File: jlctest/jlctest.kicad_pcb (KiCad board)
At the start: 2 copper layers, 121 x 75.5 mm, 44 parts, among them Q1 MMBT5551_C2145, Q2 S8550_C105432, Q3 SI2301CDS-T1-GE3, Q4 AO3401A, Q5 D882_C9634, SW1 TS-1187A-B-A-B, U1 OP07CDR, U10 L78M05ABDT-TR, U2 TPS5430DDAR, U3 SP485EEN-L/TR, U4 W25Q128JVSIQTR, U5 LM324DT, U6 74HC595D,118, U7 SP3232EEY-L/TR, U8 AMS1117-3.3, U9 AMS1117-5.0, X1 X322516MLB4SI, X2 Q13FC1350000400, X3 X322512MSB4SI, X4 X49SM8MSD2SC, X5 X50328MSB2GI

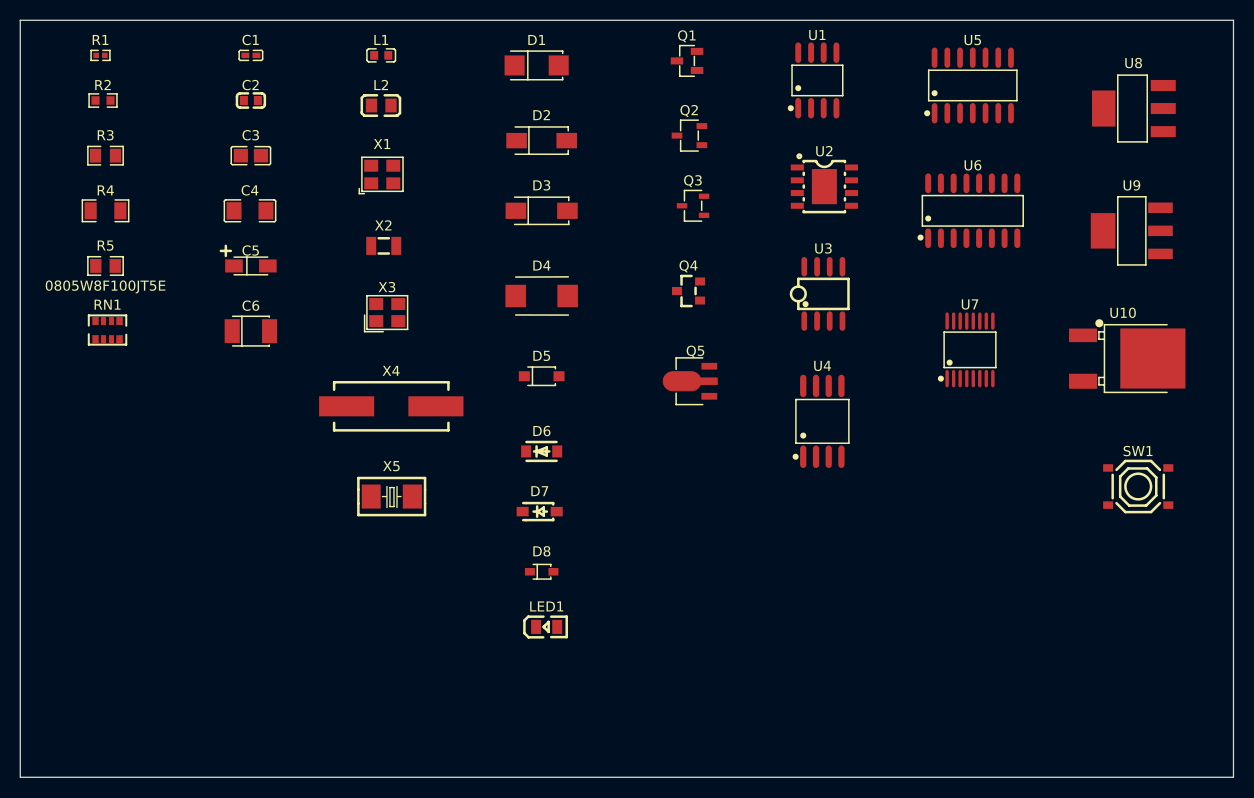
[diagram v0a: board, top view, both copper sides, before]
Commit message: Used (extends) on all symbols having an identical set of child symbols
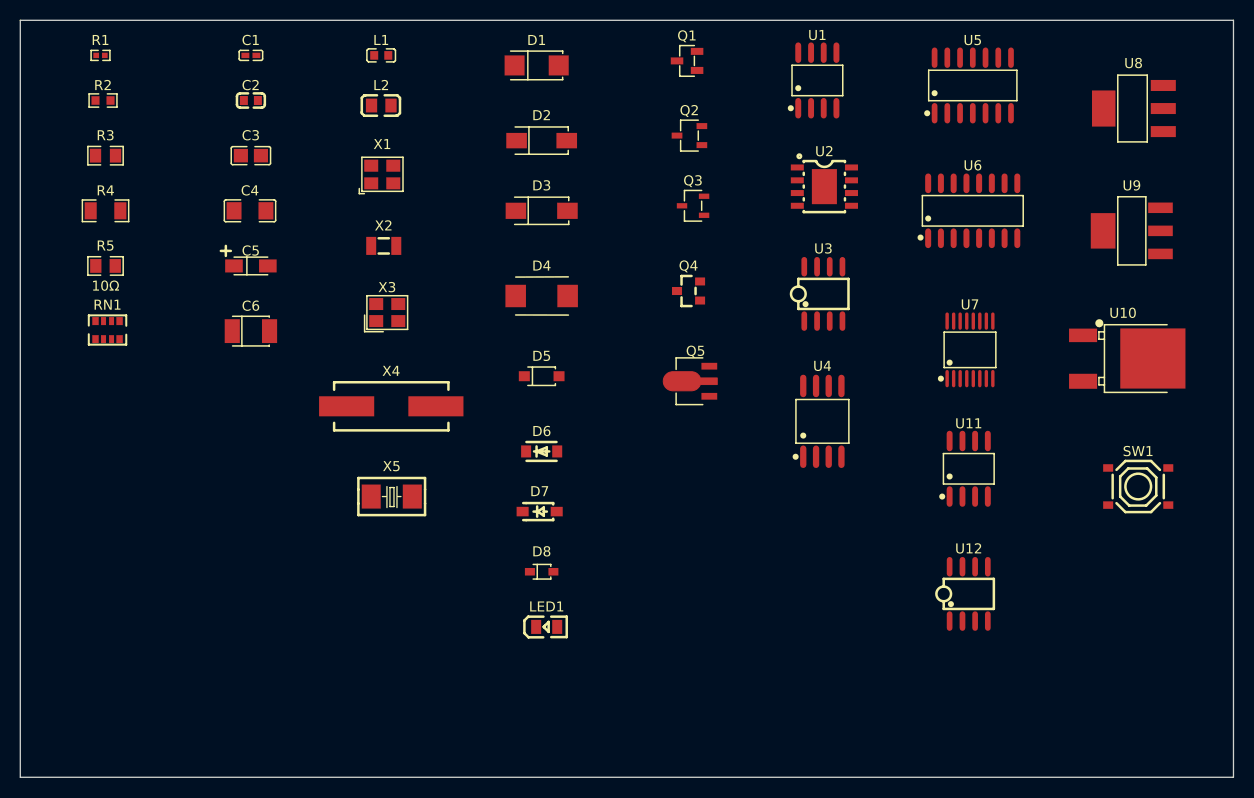
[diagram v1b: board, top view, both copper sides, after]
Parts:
- added U11: NE5532DR, jlcbasic:SOIC-8_L4.9-W3.9-P1.27-LS6.0-BL, F.Cu at (200.6, 112.7)
- added U12: TL072CDT, jlcbasic:SOIC-8_L5.0-W4.0-P1.27-LS6.0-BL, F.Cu at (200.6, 125.2)
- C1: value 0402B102K500NT -> 1nF
- C2: value 0603B103K500NT -> 10nF
- C3: value 0805B333K500NT -> 33nF
- C4: value 1206B102K202NT -> 1nF
- C5: value TAJA106K016RNJ -> 10uF
- C6: value TAJB107K006RNJ -> 100uF
- D1: value SS34_C8678 -> SS34
- D2: value SS54_C22452 -> SS54
- D3: value US1MG_C412437 -> US1MG
- D4: value P6SMB6.8CA-C78395 -> P6SMB6.8CA
- D5: value 1N4148W_C81598 -> 1N4148W
- D7: value B5819W_C8598 -> B5819W
- D8: value 1N4148WS T4 -> 1N4148ST4
- L1: value GZ1608D601TF -> 600Ω@100MHz
- L2: value GZ2012D101TF -> 100Ω@100MHz
- Q1: value MMBT5551_C2145 -> MMBT5551
- Q2: value S8550_C105432 -> S8550
- Q3: value SI2301CDS-T1-GE3 -> SI2301CDS
- Q5: value D882_C9634 -> D882
- R1: value 0402WGF0000TCE -> 0Ω
- R2: value 0603WAF0000T5E -> 0Ω
- R3: value 0805W8F0000T5E -> 0Ω
- R4: value 1206W4F0000T5E -> 0Ω
- R5: value 0805W8F100JT5E -> 10Ω
- RN1: value 4D03WGJ0102T5E -> 1KΩ
- U10: value L78M05ABDT-TR -> L78M05
- U3: value SP485EEN-L/TR -> SP485EEN
- U6: value 74HC595D,118 -> 74HC595
- U7: value SP3232EEY-L/TR -> SP3232EEY
- X1: value X322516MLB4SI -> 16MHz
- X2: value Q13FC1350000400 -> 32.768kHz
- X3: value X322512MSB4SI -> 12MHz
- X4: value X49SM8MSD2SC -> 8MHz
- X5: value X50328MSB2GI -> 8MHz
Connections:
- X1 pad 3: unconnected-(X1-OSC2-Pad3) -> (no net)
- X1 pad 4: unconnected-(X1-GND-Pad4) -> (no net)
- X3 pad 3: unconnected-(X3-OSC2-Pad3) -> (no net)
- X3 pad 4: unconnected-(X3-GND-Pad4) -> (no net)
